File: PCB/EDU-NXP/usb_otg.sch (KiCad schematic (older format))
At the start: 11 parts, among them J6 ZX62-AB-5PA, U10 MIC2025-2YM, U9 PRTR5V0U2X

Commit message: Versión completa del esquemático con todos los componentes ya definidos
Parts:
- removed C33: 100nF, ~, symbol C
- removed R48, R49: 10k, ~, symbol R
- removed U10: MIC2025-2YM, symbol MIC2025
- renumbered C31 to C3, C32 to C4, FB15 to FB1, FB1 to FB2, J6 to J2, TR2 to TR1, U9 to U2
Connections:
- net labels removed: +3.3V, +5V, USB0_PPWR, USB0_PWR_FAULT
- wire segments 57 -> 38
- no-connect marks 4 -> 2
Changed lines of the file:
@@
 Sheet 3 7
 Title "EDU CIAA USB OTG"
-Date "14 jun 2014"
+Date "24 jun 2014"
 Rev "1.0"
 Comp ""
@@
 Comment4 ""
 $EndDescr
-$Comp
-L MIC2025 U10
-U 1 1 52BC30A4
-P 2900 4700
-F 0 "U10" H 2850 5300 60  0000 L CNN
-F 1 "MIC2025-2YM" H 2600 4100 60  0000 L CNN
-F 2 "" H 2900 4700 60  0000 C CNN
-F 3 "" H 2900 4700 60  0000 C CNN
-	1    2900 4700
-	1    0    0    -1
-$EndComp
 Text HLabel 1600 3300 0    60   Output ~ 0
 USB_VBUS
@@
 Text HLabel 1600 3750 0    60   Output ~ 0
 USB_ID
-Text HLabel 1600 3900 0    60   Input ~ 0
-USB0_PPWR
-Text HLabel 1600 4050 0    60   Input ~ 0
-USB0_PWR_FAULT
-Wire Wire Line
-	1600 3900 1900 3900
-Wire Wire Line
-	1900 3900 1900 4400
-Wire Wire Line
-	1700 4400 2150 4400
-Wire Wire Line
-	1600 4050 1750 4050
-Wire Wire Line
-	1750 4050 1750 4600
-Wire Wire Line
-	1700 4600 2150 4600
-Wire Wire Line
-	2150 4800 1750 4800
-Wire Wire Line
-	1750 4800 1750 5000
-Wire Wire Line
-	2150 5000 2050 5000
-NoConn ~ 2050 5000
-$Comp
-L GND #PWR010
-U 1 1 52BC3261
-P 1750 5000
-F 0 "#PWR010" H 1750 5000 30  0001 C CNN
-F 1 "GND" H 1750 4930 30  0001 C CNN
-F 2 "" H 1750 5000 60  0000 C CNN
-F 3 "" H 1750 5000 60  0000 C CNN
-	1    1750 5000
-	1    0    0    -1
-$EndComp
-Wire Wire Line
-	3650 5000 3750 5000
-NoConn ~ 3750 5000
-$Comp
-L +5V #PWR011
-U 1 1 52BC3276
-P 3950 4500
-F 0 "#PWR011" H 3950 4590 20  0001 C CNN
-F 1 "+5V" H 3950 4590 30  0000 C CNN
-F 2 "" H 3950 4500 60  0000 C CNN
-F 3 "" H 3950 4500 60  0000 C CNN
-	1    3950 4500
-	1    0    0    -1
-$EndComp
-Wire Wire Line
-	3650 4600 3950 4600
-Connection ~ 3950 4600
-$Comp
-L GND #PWR012
-U 1 1 52BC329E
-P 3950 5250
-F 0 "#PWR012" H 3950 5250 30  0001 C CNN
-F 1 "GND" H 3950 5180 30  0001 C CNN
-F 2 "" H 3950 5250 60  0000 C CNN
-F 3 "" H 3950 5250 60  0000 C CNN
-	1    3950 5250
-	1    0    0    -1
-$EndComp
-Wire Wire Line
-	3800 4800 3650 4800
-Wire Wire Line
-	3800 4400 3650 4400
-Connection ~ 3800 4400
-$Comp
-L PRTR5V0U2X U9
+$Comp
+L PRTR5V0U2X U2
 U 1 1 52BC3F78
 P 5800 4650
-F 0 "U9" H 5800 4950 70  0000 C CNN
+F 0 "U2" H 5800 4950 70  0000 C CNN
 F 1 "PRTR5V0U2X" H 5800 4300 70  0000 C CNN
 F 2 "~" H 7350 4000 60  0000 C CNN
@@
 $EndComp
 $Comp
-L GND #PWR013
+L GND #PWR010
 U 1 1 52BC3F9D
 P 5150 5000
-F 0 "#PWR013" H 5150 5000 30  0001 C CNN
+F 0 "#PWR010" H 5150 5000 30  0001 C CNN
 F 1 "GND" H 5150 4930 30  0001 C CNN
 F 2 "" H 5150 5000 60  0000 C CNN
@@
 	1    0    0    -1
 $EndComp
-Connection ~ 3800 3300
 Wire Wire Line
 	6450 3300 6450 4550
@@
 	5150 4550 5350 4550
 $Comp
-L CAPAPOL C31
+L CAPAPOL C3
 U 1 1 52BC4098
 P 7200 4650
-F 0 "C31" H 7250 4750 40  0000 L CNN
+F 0 "C3" H 7250 4750 40  0000 L CNN
 F 1 "10uF" H 7250 4550 40  0000 L CNN
 F 2 "~" H 7300 4500 30  0000 C CNN
@@
 $EndComp
 $Comp
-L C C32
+L C C4
 U 1 1 52BC40A7
 P 7550 4650
-F 0 "C32" H 7550 4750 40  0000 L CNN
+F 0 "C4" H 7550 4750 40  0000 L CNN
 F 1 "100nF" H 7556 4565 40  0000 L CNN
 F 2 "~" H 7588 4500 30  0000 C CNN
@@
 	7550 4950 7550 4850
 $Comp
-L GND #PWR014
+L GND #PWR011
 U 1 1 52BC411A
 P 7550 4950
-F 0 "#PWR014" H 7550 4950 30  0001 C CNN
+F 0 "#PWR011" H 7550 4950 30  0001 C CNN
 F 1 "GND" H 7550 4880 30  0001 C CNN
 F 2 "" H 7550 4950 60  0000 C CNN
@@
 $EndComp
 $Comp
-L GND #PWR015
+L GND #PWR012
 U 1 1 52BC4129
 P 7200 4950
-F 0 "#PWR015" H 7200 4950 30  0001 C CNN
+F 0 "#PWR012" H 7200 4950 30  0001 C CNN
 F 1 "GND" H 7200 4880 30  0001 C CNN
 F 2 "" H 7200 4950 60  0000 C CNN
@@
 Connection ~ 5250 3450
 $Comp
-L CONN_9 J6
+L CONN_9 J2
 U 1 1 52BC445A
 P 10500 3700
-F 0 "J6" V 10450 3700 60  0000 C CNN
+F 0 "J2" V 10450 3700 60  0000 C CNN
 F 1 "ZX62-AB-5PA" V 10550 3700 60  0000 C CNN
 F 2 "" H 10500 3700 60  0000 C CNN
@@
 	9700 3700 9700 4950
 $Comp
-L GND #PWR016
+L GND #PWR013
 U 1 1 52BC45E9
 P 9700 4950
-F 0 "#PWR016" H 9700 4950 30  0001 C CNN
+F 0 "#PWR013" H 9700 4950 30  0001 C CNN
 F 1 "GND" H 9700 4880 30  0001 C CNN
 F 2 "" H 9700 4950 60  0000 C CNN
@@
 	10150 3900 10050 3900
 Connection ~ 10050 3900
-$Comp
-L C C33
-U 1 1 52BC4969
-P 3950 4900
-F 0 "C33" H 3950 5000 40  0000 L CNN
-F 1 "100nF" H 3956 4815 40  0000 L CNN
-F 2 "~" H 3988 4750 30  0000 C CNN
-F 3 "~" H 3950 4900 60  0000 C CNN
-	1    3950 4900
-	1    0    0    -1
-$EndComp
-Wire Wire Line
-	3950 5250 3950 5100
-Wire Wire Line
-	3950 4500 3950 4700
 Connection ~ 6450 3300
 Wire Wire Line
@@
 Connection ~ 9700 4900
 $Comp
-L FILTER FB1
+L FILTER FB2
 U 1 1 52C75800
 P 10050 4500
-F 0 "FB1" H 10050 4650 60  0000 C CNN
+F 0 "FB2" H 10050 4650 60  0000 C CNN
 F 1 "MMZ1608B601C" H 10050 4400 60  0000 C CNN
 F 2 "~" H 10050 4500 60  0000 C CNN
@@
 $EndComp
 $Comp
-L R R49
-U 1 1 52C9D8D3
-P 1450 4600
-F 0 "R49" V 1530 4600 40  0000 C CNN
-F 1 "10k" V 1457 4601 40  0000 C CNN
-F 2 "~" V 1380 4600 30  0000 C CNN
-F 3 "~" H 1450 4600 30  0000 C CNN
-	1    1450 4600
-	0    -1   -1   0
-$EndComp
-Connection ~ 1750 4600
-$Comp
-L +3.3V #PWR017
-U 1 1 52C9D999
-P 1150 4600
-F 0 "#PWR017" H 1150 4560 30  0001 C CNN
-F 1 "+3.3V" H 1150 4710 30  0000 C CNN
-F 2 "" H 1150 4600 60  0000 C CNN
-F 3 "" H 1150 4600 60  0000 C CNN
-	1    1150 4600
-	0    -1   -1   0
-$EndComp
-Wire Wire Line
-	1150 4600 1200 4600
-$Comp
-L R R48
-U 1 1 52C9D9F8
-P 1450 4400
-F 0 "R48" V 1530 4400 40  0000 C CNN
-F 1 "10k" V 1457 4401 40  0000 C CNN
-F 2 "~" V 1380 4400 30  0000 C CNN
-F 3 "~" H 1450 4400 30  0000 C CNN
-	1    1450 4400
-	0    -1   -1   0
-$EndComp
-$Comp
-L GND #PWR018
-U 1 1 52C9DA03
-P 1150 4450
-F 0 "#PWR018" H 1150 4450 30  0001 C CNN
-F 1 "GND" H 1150 4380 30  0001 C CNN
-F 2 "" H 1150 4450 60  0000 C CNN
-F 3 "" H 1150 4450 60  0000 C CNN
-	1    1150 4450
-	1    0    0    -1
-$EndComp
-Wire Wire Line
-	1150 4450 1150 4400
-Wire Wire Line
-	1150 4400 1200 4400
-Connection ~ 1900 4400
-$Comp
-L FILTER FB15
+L FILTER FB1
 U 1 1 52DDB16D
 P 8200 3300
-F 0 "FB15" H 8200 3200 60  0000 C CNN
+F 0 "FB1" H 8200 3200 60  0000 C CNN
 F 1 "BLM18KG221SN1" H 8200 3100 60  0000 C CNN
 F 2 "~" H 8200 3300 60  0000 C CNN
@@
 	1600 3300 7850 3300
 $Comp
-L TRASF_UNIP TR2
+L TRASF_UNIP TR1
 U 1 1 52DDB29E
 P 8200 4100
-F 0 "TR2" V 8600 4100 60  0000 C CNN
+F 0 "TR1" V 8600 4100 60  0000 C CNN
 F 1 "DLW21HN900SQ2" V 8500 4100 60  0000 C CNN
 F 2 "" H 8200 4100 60  0000 C CNN
@@
 Wire Wire Line
 	7950 4300 8050 4300
-Wire Wire Line
-	3800 3300 3800 4800
 NoConn ~ 10150 4000
 NoConn ~ 10150 4100

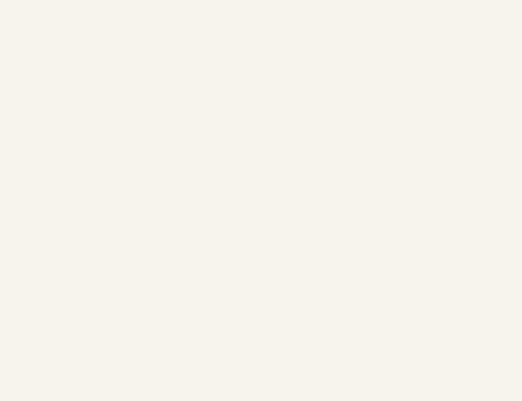
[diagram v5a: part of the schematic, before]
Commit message: PCB V0.0 finalizado - Se agregaron planos de masa, control de dimensiones y perforaciones, se agregó el LOGO
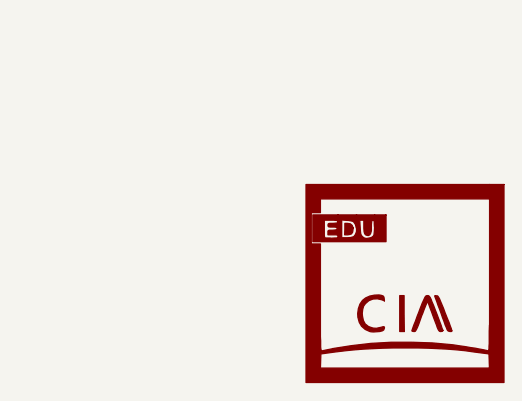
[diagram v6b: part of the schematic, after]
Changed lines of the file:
@@
 LIBS:pbss5240xf
 LIBS:LED_RGB
+LIBS:Logo
 LIBS:edu-ciaa-nxp-cache
 EELAYER 27 0
@@
 Sheet 3 7
 Title "EDU CIAA USB OTG"
-Date "12 jul 2014"
+Date "14 jul 2014"
 Rev "1.0"
 Comp ""
@@
 NoConn ~ 10150 4000
 NoConn ~ 10150 4100
+$Comp
+L LOGO #G3
+U 1 1 53C3FC54
+P 10650 6600
+F 0 "#G3" H 10650 6197 60  0001 C CNN
+F 1 "LOGO" H 10650 7003 60  0001 C CNN
+F 2 "" H 10650 6600 60  0000 C CNN
+F 3 "" H 10650 6600 60  0000 C CNN
+	1    10650 6600
+	1    0    0    -1
+$EndComp
 $EndSCHEMATC

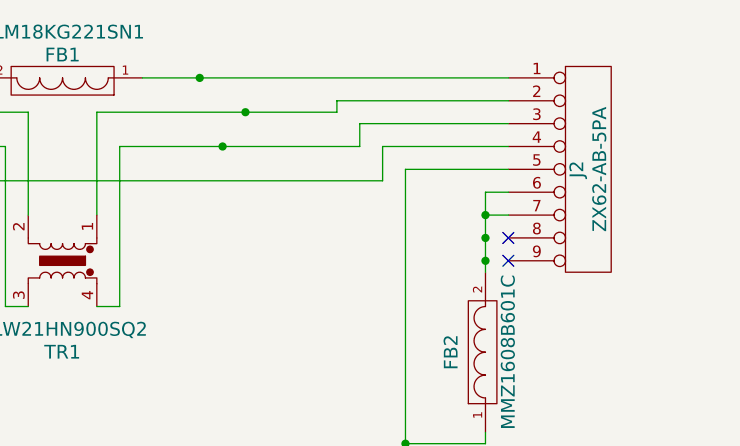
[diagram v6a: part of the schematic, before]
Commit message: Teclas THT y conectores micro USB THT
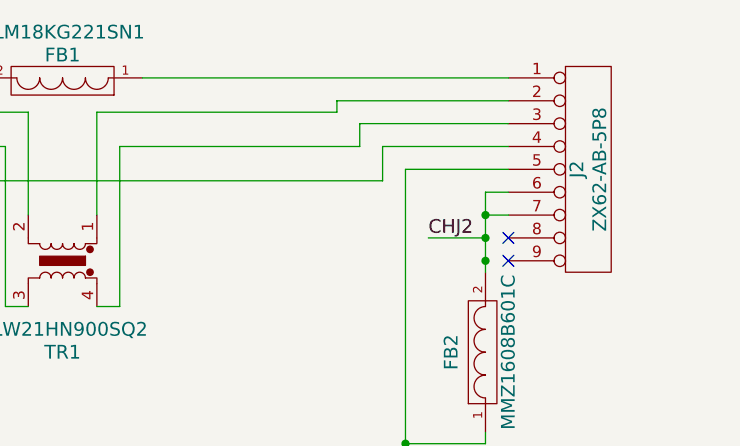
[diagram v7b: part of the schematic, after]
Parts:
- J2: value ZX62-AB-5PA -> ZX62-AB-5P8
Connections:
- net CHJ2: now reaches FB2.2, J2.6 (P6), J2.7 (P7)
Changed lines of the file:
@@
 LIBS:LED_RGB
 LIBS:Logo
+LIBS:edu-ciaa-logo
 LIBS:edu-ciaa-nxp-cache
 EELAYER 27 0
@@
 Sheet 3 7
 Title "EDU CIAA USB OTG"
-Date "14 jul 2014"
+Date "17 jul 2014"
 Rev "1.0"
 Comp ""
@@
 P 10500 3700
 F 0 "J2" V 10450 3700 60  0000 C CNN
-F 1 "ZX62-AB-5PA" V 10550 3700 60  0000 C CNN
+F 1 "ZX62-AB-5P8" V 10550 3700 60  0000 C CNN
 F 2 "" H 10500 3700 60  0000 C CNN
 F 3 "" H 10500 3700 60  0000 C CNN
@@
 	1    0    0    -1
 $EndComp
-Connection ~ 8800 3300
 Wire Wire Line
 	10150 3400 9400 3400
 Wire Wire Line
 	9400 3400 9400 3450
-Connection ~ 9000 3450
 Wire Wire Line
 	10150 3500 9500 3500
 Wire Wire Line
 	9500 3500 9500 3600
-Connection ~ 8900 3600
 Wire Wire Line
 	10150 3600 9600 3600
@@
 	1    0    0    -1
 $EndComp
+Wire Wire Line
+	10050 4000 9800 4000
+Text Label 9800 4000 0    60   ~ 0
+CHJ2
 $EndSCHEMATC

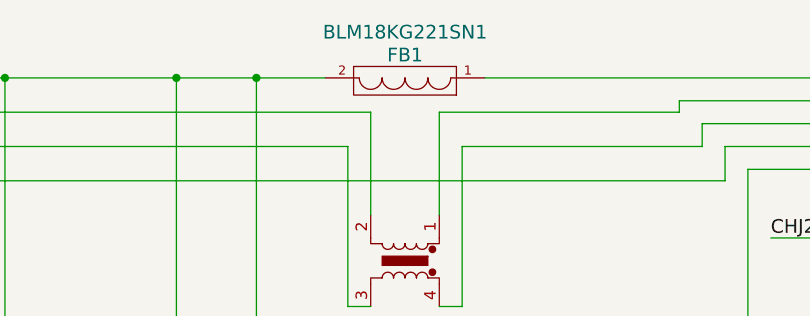
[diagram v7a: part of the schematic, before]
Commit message: Cambio de filtros en 0603 por MI0805M221R-10 (encapsulado 0805)
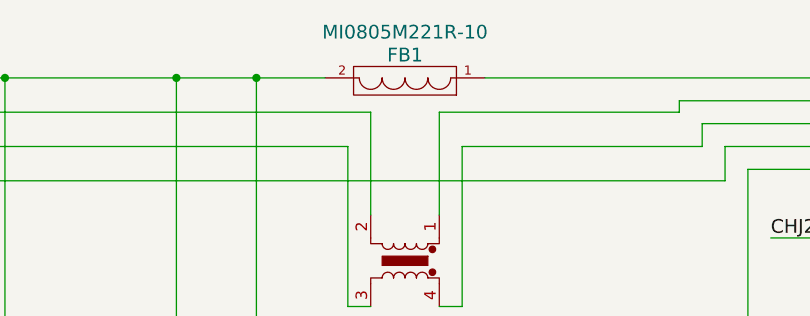
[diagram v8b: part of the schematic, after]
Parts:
- FB1: value BLM18KG221SN1 -> MI0805M221R-10
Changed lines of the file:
@@
 Sheet 3 7
 Title "EDU CIAA USB OTG"
-Date "17 jul 2014"
+Date "23 jul 2014"
 Rev "1.0"
 Comp ""
@@
 P 8200 3300
 F 0 "FB1" H 8200 3200 60  0000 C CNN
-F 1 "BLM18KG221SN1" H 8200 3100 60  0000 C CNN
+F 1 "MI0805M221R-10" H 8200 3100 60  0000 C CNN
 F 2 "~" H 8200 3300 60  0000 C CNN
 F 3 "~" H 8200 3300 60  0000 C CNN
